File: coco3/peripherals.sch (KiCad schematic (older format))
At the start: 59 parts, among them CN2 Conn_01x16_Female, IC14 74LS30, IC15 74LS04, IC4 W65C21N6TPG-14, IC5 W65C21N6TPG-14, IC7 SC77526, IC8 SC77527P, Q1 2N6123

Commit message: -replaced PIA's with he PLCC44 package versions -removed RF modulator -removed DRAM
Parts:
- removed IC4: W65C21N6TPG-14, Package_DIP:DIP-40_W15.24mm_Socket, symbol Interface:6821
- removed IC5: W65C21N6TPG-14, Package_DIP:DIP-40_W15.24mm_Socket, symbol Interface:6822
- added IC4, IC5: W65C21N6TPLG-14, Package_LCC:PLCC-44_THT-Socket, symbol coco2:W65C21N6TPLG-14
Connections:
- net labels added: CASS_DATA_IN_TTL, CASS_M_ON_TTL, CD_IN_RS232, CD_IN_TTL, K15, SERIAL_DATA_IN_RS232, SERIAL_IN_TTL, SERIAL_OUT_RS232, SER_OUT_TTL
- net labels removed: CASS_DATA_OUT_TTL, CASS_M_IN_TTL, CD_IN, CD_OUT_TTL, SERIAL_DATA_IN, SER_DATA_IN_TTL, SER_DATA_OUT, SER_DATA_OUT_TTL
- wire segments 334 -> 349
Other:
- moved on the sheet: C6, C7, IC15B, R12, R59, R6, R7

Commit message: -repplaced a whole bunch of THT components with SMT components
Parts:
- C13, C14, C47, C48, C6, C7: footprint Capacitor_THT:C_Disc_D4.7mm_W2.5mm_P5.00mm -> Capacitor_SMD:C_0805_2012Metric_Pad1.18x1.45mm_HandSolder; Manufacturer part# FG28C0G1H103JNT06 -> CL21A106KAYNNNE; Vendor digikey -> JLCPCB; Vendor part# 445-173474-1-ND -> C15850
- C15: footprint Capacitor_THT:CP_Radial_D8.0mm_P5.00mm -> Capacitor_SMD:CP_Elec_6.3x5.3; Manufacturer part# UST1C101MDD1TA -> VEJ101M1CTR-0605; Vendor digikey -> JLCPCB; Vendor part# 493-17434-1-ND -> C164064
- C16, C17, C20, C21, C25, C49: footprint Capacitor_THT:C_Disc_D8.0mm_W2.5mm_P5.00mm -> Capacitor_SMD:C_0805_2012Metric_Pad1.18x1.45mm_HandSolder; Manufacturer part# C317C223M5U5TA7301 -> CL21B223KBANNNC; Vendor digikey -> JLCPCB; Vendor part# 399-14073-1-ND -> C1729
- C18, C19, C22, C23: footprint Capacitor_THT:C_Disc_D4.7mm_W2.5mm_P5.00mm -> Capacitor_SMD:C_0805_2012Metric_Pad1.18x1.45mm_HandSolder; Manufacturer part# FA28C0G1H182JNU06 -> 0805B182K500NT; Vendor digikey -> JLCPCB; Vendor part# 445-180714-1-ND -> C1722
- IC14: footprint Package_DIP:DIP-14_W7.62mm_Socket -> Package_SO:SOIC-14_3.9x8.7mm_P1.27mm; Manufacturer part# SN74LS30N -> SN74LS30DR; Vendor digikey -> JLCPCB; Vendor part# 296-3693-5-ND -> C7759
- IC15: footprint Package_DIP:DIP-14_W7.62mm_Socket -> Package_SO:SOIC-14_3.9x8.7mm_P1.27mm; Manufacturer part# SN74LS04N -> SN74LS04DR; Vendor digikey -> JLCPCB; Vendor part# 296-1629-5-ND -> C6796
- R15: footprint Resistor_THT:R_Axial_DIN0204_L3.6mm_D1.6mm_P7.62mm_Horizontal -> Resistor_SMD:R_2010_5025Metric_Pad1.40x2.65mm_HandSolder; Manufacturer part# SFR16S0002700JA500 -> 2010W2J0271T4S; Vendor digikey -> JLCPCB; Vendor part# BC4316CT-ND -> C20393
- R16, R17: footprint Resistor_THT:R_Axial_DIN0207_L6.3mm_D2.5mm_P10.16mm_Horizontal -> Resistor_SMD:R_1206_3216Metric_Pad1.30x1.75mm_HandSolder; Manufacturer part# CF14JT1K00 -> 1206W4F1001T5; Vendor digikey -> JLCPCB; Vendor part# CF14JT1K00CT-ND -> C4410
- R21, R24, R59, R6, R7: footprint Resistor_THT:R_Axial_DIN0207_L6.3mm_D2.5mm_P10.16mm_Horizontal -> Resistor_SMD:R_1206_3216Metric_Pad1.30x1.75mm_HandSolder; Manufacturer part# Stackpole Electronics Inc -> 1206W4F4701T5E; Vendor digikey -> JLCPCB; Vendor part# CF14JT4K70CT-ND -> C17936

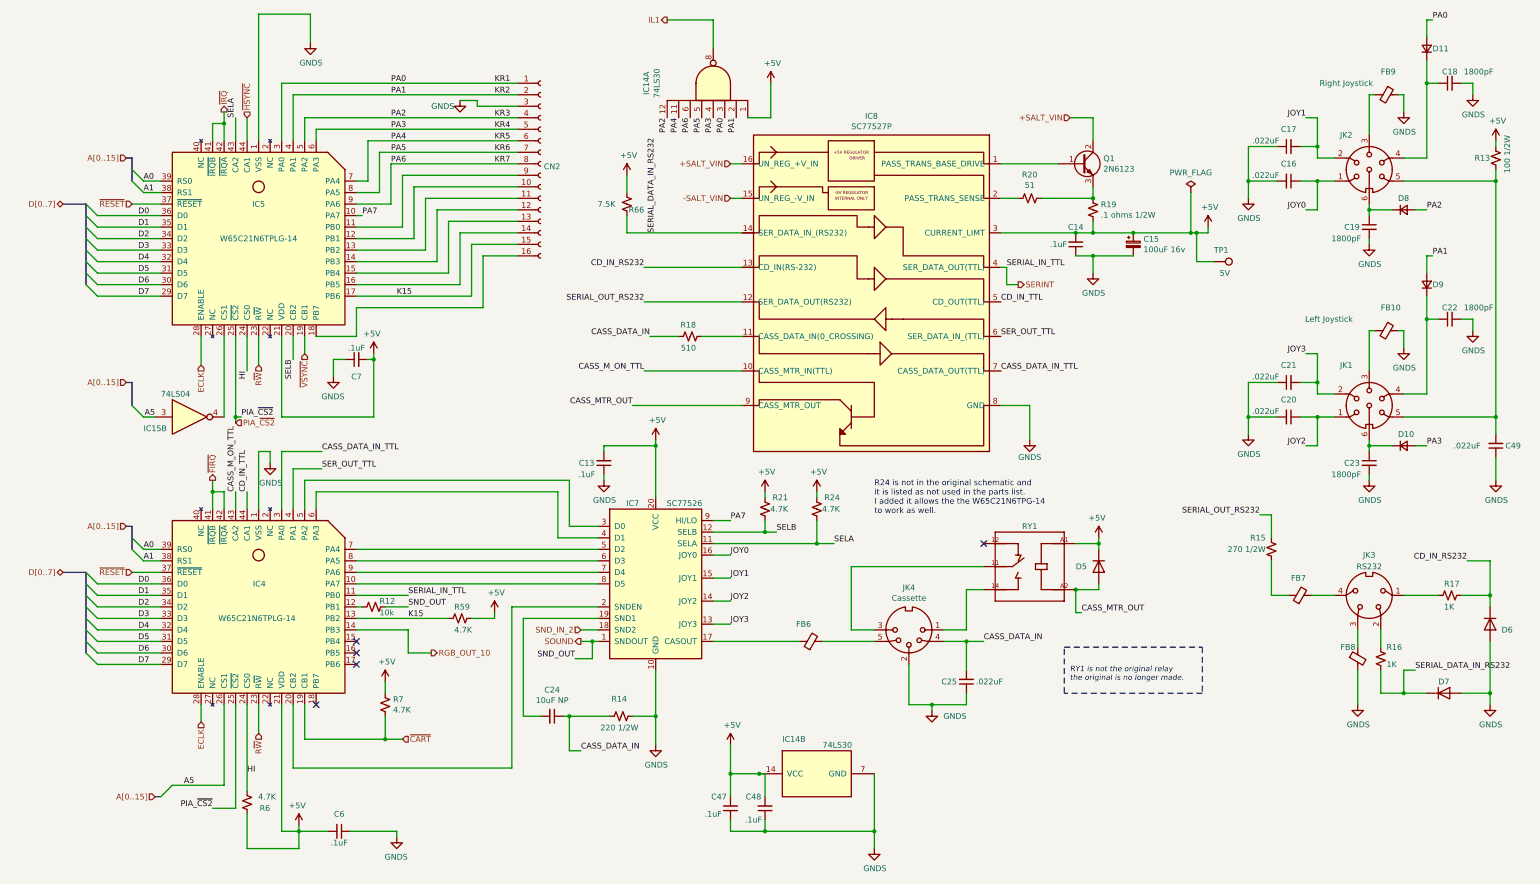
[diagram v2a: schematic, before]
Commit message: -converted more components from THT to SMD -replaced SALT chip with replacement circuitry
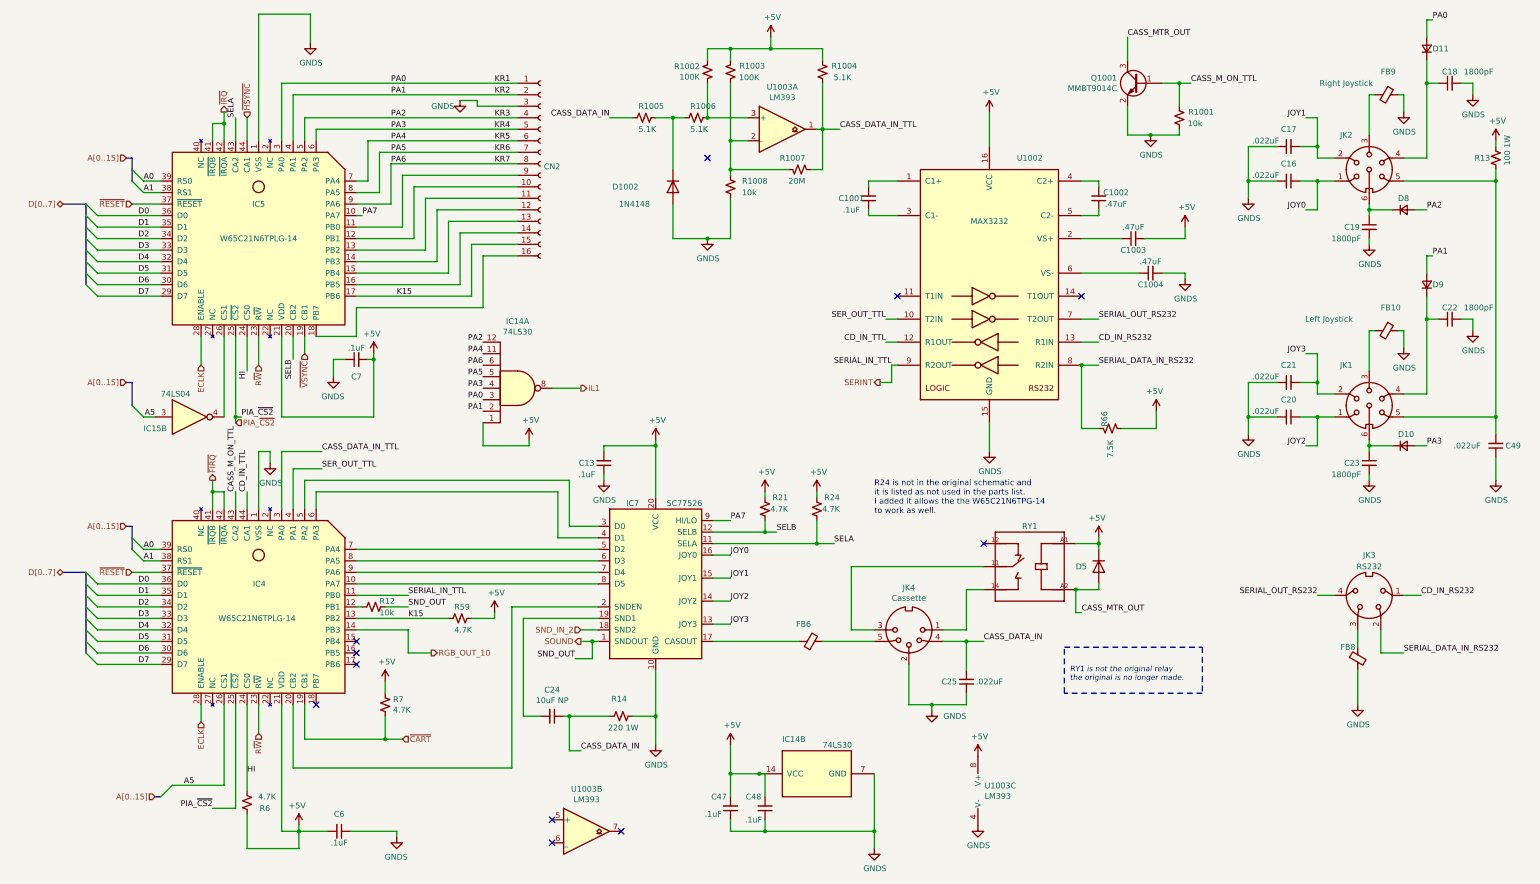
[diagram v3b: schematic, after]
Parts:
- removed C14: .1uF, Capacitor_SMD:C_0805_2012Metric_Pad1.18x1.45mm_HandSolder, symbol Device:C_Small
- removed C15: 100uF 16v, Capacitor_SMD:CP_Elec_6.3x5.3, symbol Device:CP_Small
- removed D6, D7: 1N5228B-TAP, Diode_THT:D_DO-35_SOD27_P7.62mm_Horizontal, symbol Diode:1N4148
- removed FB7: (no value), coco2:FB_28L0138-10R-10, symbol Device:Ferrite_Bead_Small
- removed IC8: SC77527P, Package_DIP:DIP-16_W7.62mm_Socket, symbol coco2:SC77527P
- removed Q1: 2N6123, Package_TO_SOT_THT:TO-220-3_Horizontal_TabDown, symbol Device:Q_NPN_BCE
- removed R15: 270 1/2W, Resistor_SMD:R_2010_5025Metric_Pad1.40x2.65mm_HandSolder, symbol Device:R_Small_US
- removed R16, R17: 1K, Resistor_SMD:R_1206_3216Metric_Pad1.30x1.75mm_HandSolder, symbol Device:R_Small_US
- removed R18: 510, Resistor_THT:R_Axial_DIN0207_L6.3mm_D2.5mm_P10.16mm_Horizontal, symbol Device:R_Small_US
- removed R19: .1 ohms 1/2W, Resistor_THT:R_Axial_DIN0411_L9.9mm_D3.6mm_P15.24mm_Horizontal, symbol Device:R_Small_US
- removed R20: 51, Resistor_THT:R_Axial_DIN0207_L6.3mm_D2.5mm_P10.16mm_Horizontal, symbol Device:R_Small_US
- removed TP1: 5V, TestPoint:TestPoint_Pad_3.0x3.0mm, symbol Connector:TestPoint
- added C1001: .1uF, Capacitor_SMD:C_0805_2012Metric_Pad1.18x1.45mm_HandSolder, symbol Device:C_Small
- added C1002, C1003, C1004: .47uF, Capacitor_SMD:C_0805_2012Metric_Pad1.18x1.45mm_HandSolder, symbol Device:C_Small
- added D1002: 1N4148, Diode_SMD:D_SOD-323F, symbol Diode:1N4148
- added Q1001: MMBT9014C, Package_TO_SOT_SMD:SOT-23, symbol Device:Q_NPN_BEC
- added R1001, R1008: 10k, Resistor_SMD:R_1206_3216Metric_Pad1.30x1.75mm_HandSolder, symbol Device:R_Small_US
- added R1002, R1003: 100K, Resistor_SMD:R_1206_3216Metric_Pad1.30x1.75mm_HandSolder, symbol Device:R_Small_US
- added R1004, R1005, R1006: 5.1K, Resistor_SMD:R_1206_3216Metric_Pad1.30x1.75mm_HandSolder, symbol Device:R_Small_US
- added R1007: 20M, Resistor_SMD:R_1206_3216Metric_Pad1.30x1.75mm_HandSolder, symbol Device:R_Small_US
- added U1002: MAX3232, Package_SO:SOIC-16_3.9x9.9mm_P1.27mm, symbol Interface_UART:MAX3232
- added U1003: LM393, Package_SO:TSSOP-8_4.4x3mm_P0.65mm, symbol Comparator:LM393
- D5: footprint Diode_THT:D_DO-35_SOD27_P7.62mm_Horizontal -> Diode_SMD:D_SOD-323F; Manufacturer part# 1N4148 -> 1N4148WS; Vendor digikey -> JLCPCB; Vendor part# 1N4148FS-ND -> C2128
- R12: footprint Resistor_THT:R_Axial_DIN0207_L6.3mm_D2.5mm_P10.16mm_Horizontal -> Resistor_SMD:R_1206_3216Metric_Pad1.30x1.75mm_HandSolder; Manufacturer part# CF14JT10K0 -> 1206W4F1002T5E; Vendor digikey -> JLCPCB; Vendor part# CF14JT10K0CT-ND -> C17902
- R13: value 100 1/2W -> 100 1W; footprint Resistor_THT:R_Axial_DIN0411_L9.9mm_D3.6mm_P12.70mm_Horizontal -> Resistor_SMD:R_2512_6332Metric_Pad1.40x3.35mm_HandSolder; Manufacturer part# CF12JT100R -> 25121WF1000T4E; Vendor digikey -> JLCPCB; Vendor part# CF12JT100RCT-ND -> C35218
- R14: value 220 1/2W -> 220 1W; footprint Resistor_THT:R_Axial_DIN0411_L9.9mm_D3.6mm_P12.70mm_Horizontal -> Resistor_SMD:R_2512_6332Metric_Pad1.40x3.35mm_HandSolder; Manufacturer part# CF12JT220R -> 25121WJ0221T4E; Vendor digikey -> JLCPCB; Vendor part# CF12JT220RCT-ND -> C38808
- R66: footprint Resistor_THT:R_Axial_DIN0207_L6.3mm_D2.5mm_P10.16mm_Horizontal -> Resistor_SMD:R_1206_3216Metric_Pad1.30x1.75mm_HandSolder; Manufacturer part# RNF14FTD7K50 -> 1206W4F7501T5E; Vendor digikey -> JLCPCB; Vendor part# RNF14FTD7K50CT-ND -> C17978
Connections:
- net +5V: now also C1003.2, R1002.1, R1003.1, R1004.2, U1002.16 (VCC), U1003.8 (V+)
- net CASS_DATA_IN: now also R1005.2
- net CASS_DATA_IN_TTL: now also R1004.1, R1007.2, U1003.1
- net CASS_MTR_OUT: now also Q1001.3 (C)
- net CASS_M_ON_TTL: now also Q1001.1 (B), R1001.2
- net CD_IN_RS232: now also JK3.1, U1002.13 (R1IN)
- net CD_IN_TTL: now also U1002.12 (R1OUT)
- net GNDS: now also C1004.2, D1002.2 (A), Q1001.2 (E), R1001.1, R1008.2, U1002.15 (GND), U1003.4 (V-)
- net SERIAL_DATA_IN_RS232: now also JK3.2, U1002.8 (R2IN)
- net SERIAL_OUT_RS232: now also JK3.4, U1002.7 (T2OUT)
- net SERINT: now also U1002.9 (R2OUT)
- net SER_OUT_TTL: now also U1002.10 (T2IN)
- new net: C1001.2, U1002.1 (C1+)
- new net: C1003.1, U1002.2 (VS+)
- new net: C1001.1, U1002.3 (C1-)
- new net: C1002.2, U1002.4 (C2+)
- new net: C1002.1, U1002.5 (C2-)
- new net: C1004.1, U1002.6 (VS-)
- new net: R1003.2, R1007.1, R1008.1, U1003.2 (-)
- new net: R1002.2, R1006.1, U1003.3 (+)
- new net: D1002.1 (K), R1005.1, R1006.2
- no-connect marks 5 -> 11
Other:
- moved on the sheet: IC14A, R66

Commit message: routed the board
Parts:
- added BREAKOUT0: Conn_01x18_Male, Connector_PinHeader_2.54mm:PinHeader_1x18_P2.54mm_Vertical, symbol Connector:Conn_01x18_Male
- added J1002: Conn_01x04_Male, Connector_PinHeader_2.54mm:PinHeader_1x04_P2.54mm_Vertical, symbol Connector:Conn_01x04_Male
- R1004, R1005, R1006: footprint Resistor_SMD:R_1206_3216Metric_Pad1.30x1.75mm_HandSolder -> Resistor_SMD:R_0805_2012Metric_Pad1.20x1.40mm_HandSolder; Manufacturer part# 1206W4F5101T5E -> 0805W8F5101T5E; Vendor part# C26033 -> C27834
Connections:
- net +5V: now also BREAKOUT0.18 (Pin_18)
- net GNDS: now also BREAKOUT0.17 (Pin_17), BREAKOUT0.3 (Pin_3)
- net K15: now also BREAKOUT0.15 (Pin_15)
- net KR1: now also BREAKOUT0.1 (Pin_1)
- net KR2: now also BREAKOUT0.2 (Pin_2)
- net KR3: now also BREAKOUT0.4 (Pin_4)
- net KR4: now also BREAKOUT0.5 (Pin_5)
- net KR5: now also BREAKOUT0.6 (Pin_6)
- net KR6: now also BREAKOUT0.7 (Pin_7)
- net KR7: now also BREAKOUT0.8 (Pin_8)
- net at CN2.10 (Pin_10), IC5.12 (PB1): now also BREAKOUT0.10 (Pin_10)
- net at CN2.11 (Pin_11), IC5.13 (PB2): now also BREAKOUT0.11 (Pin_11)
- net at CN2.12 (Pin_12), IC5.14 (PB3): now also BREAKOUT0.12 (Pin_12)
- net at CN2.13 (Pin_13), IC5.15 (PB4): now also BREAKOUT0.13 (Pin_13)
- net at CN2.14 (Pin_14), IC5.16 (PB5): now also BREAKOUT0.14 (Pin_14)
- net at CN2.16 (Pin_16), IC5.18 (PB7): now also BREAKOUT0.16 (Pin_16)
- net at CN2.9 (Pin_9), IC5.11 (PB0): now also BREAKOUT0.9 (Pin_9)
- net IC4_PB4: now reaches IC4.15 (PB4)
- net IC4_PB4: now also J1002.1 (Pin_1)
- net IC4_PB5: now reaches IC4.16 (PB5)
- net IC4_PB5: now also J1002.2 (Pin_2)
- net IC4_PB6: now reaches IC4.17 (PB6)
- net IC4_PB6: now also J1002.3 (Pin_3)
- net IC4_PB7: now reaches IC4.18 (PB7)
- net IC4_PB7: now also J1002.4 (Pin_4)
- no-connect marks 11 -> 7
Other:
- note added: "There are two connectors here.\nThe keyboard connector and a \nbreakout header."
- moved on the sheet: D1002, R1002, R1003, R1004, R1005, R1006, R1007, R1008, R7, U1003A
